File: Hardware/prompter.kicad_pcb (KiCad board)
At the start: 4 copper layers, 99.7 x 70.1 mm, 106 parts, among them J1 USB_B_Micro, J2 SWD, J3 L1, J4 L3, J5 PWR, J6 L2, J7 L4, J8 UART, J9 FootSW, Q1 AO3401A, Q2 IRLZ44N, Q3 IRLZ44N, Q4 IRLZ44N, Q5 IRLZ44N, SW1 PGM/RUN, SW2 SW_SPDT, SW3 SW_SPDT, SW4 SW_SPDT, SW5 SW_SPDT, U1 74HC14, U2 USBLC6-2P6, U3 STM32F405RGT6, U4 EL817, U5 EL817, U6 MP2359, Y1 16MHz

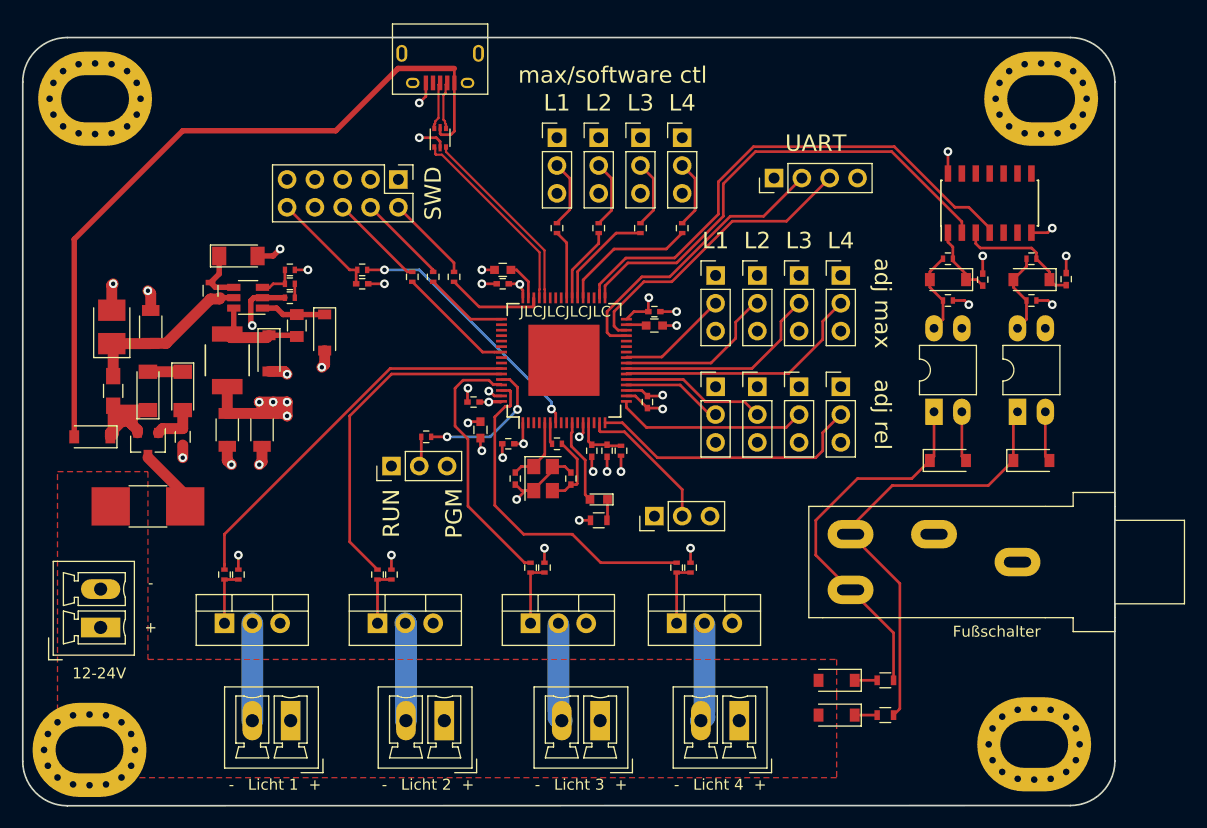
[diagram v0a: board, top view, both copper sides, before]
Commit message: for future extension, also added DMX hardware
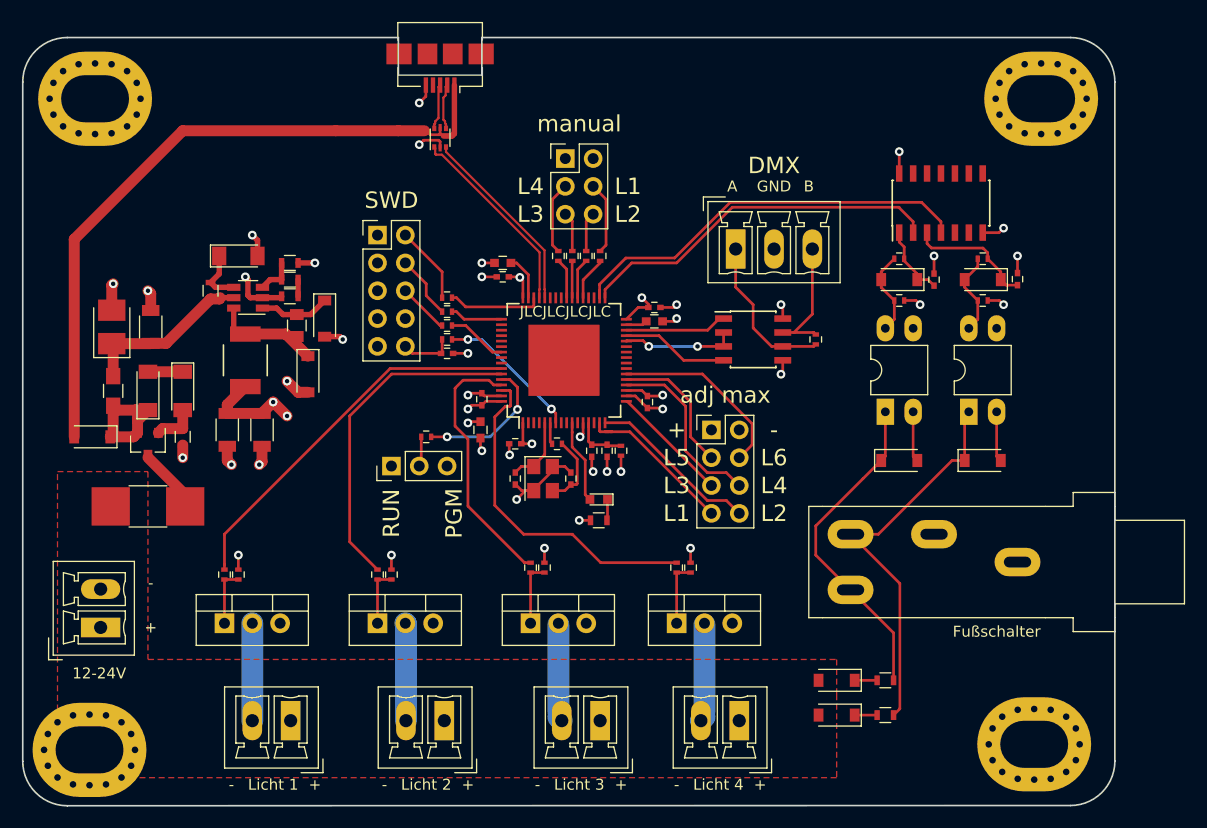
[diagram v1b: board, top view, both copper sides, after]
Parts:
- removed RV1, RV2, RV3, RV4, RV5, RV6, RV7, RV8, RV9: 10k, Pin_Headers:Pin_Header_Straight_1x03_Pitch2.54mm
- removed SW2, SW3, SW4, SW5: SW_SPDT, Pin_Headers:Pin_Header_Straight_1x03_Pitch2.54mm
- added J10: manual, Pin_Headers:Pin_Header_Straight_2x03_Pitch2.54mm, F.Cu at (74.4, 127.9)
- added J11: max, Pin_Headers:Pin_Header_Straight_2x04_Pitch2.54mm, F.Cu at (87.8, 152.7)
- added R31: 120, Resistors_SMD:R_0402, F.Cu at (97.3, 144.4)
- added U7: SP3485EN, Housings_SOIC:SOIC-8_3.9x4.9mm_Pitch1.27mm, F.Cu at (91.6, 144.4)
- J1: footprint Connectors:USB_Micro-B -> Connector_USB:USB_Micro-B_Amphenol_10104110_Horizontal
- J8: value UART -> DMX; footprint Pin_Headers:Pin_Header_Straight_1x04_Pitch2.54mm -> Connectors_Phoenix:PhoenixContact_MCV-G_03x3.50mm_Vertical
- R2, R4, R5: footprint Resistors_SMD:R_0402 -> Resistors_SMD:R_0603
- moved R13 11.6 mm to (73.8, 136.8)
- moved C6 10.0 mm to (63.6, 145.7)
- moved R9 10.0 mm to (63.6, 144.4)
- moved J8 7.36 mm to (90.0, 136.1), turned to 0 degrees
- moved R15 6.72 mm to (75.1, 136.8)
- moved R8 5.46 mm to (63.6, 143.1), turned to 180 degrees
- moved J2 5.43 mm to (57.3, 134.9), turned to 0 degrees
- moved C20 4.45 mm to (108.1, 138.9)
- moved U4 4.45 mm to (111.3, 151.0)
- moved C19 4.44 mm to (115.7, 138.9)
- moved D10 4.44 mm to (104.9, 138.9)
- moved D11 4.44 mm to (104.9, 155.4)
- moved D8 4.44 mm to (112.5, 155.4)
- moved D9 4.44 mm to (112.5, 138.9)
- moved R18 4.44 mm to (112.5, 140.8)
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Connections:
- J1 pad 4: Net-(J1-Pad4) -> (no net)
- J2 pad 7: Net-(J2-Pad7) -> (no net)
- J2 pad 8: Net-(J2-Pad8) -> (no net)
- J8 pad 1: +3V3 -> Net-(J8-Pad1)
- J8 pad 2: USART_TX -> GND
- J8 pad 3: USART_RX -> Net-(J8-Pad3)
- R13 pad 1: L1MAN -> L4MAN
- R14 pad 1: L3MAN -> L1MAN
- R15 pad 1: L2MAN -> L3MAN
- R16 pad 1: L4MAN -> L2MAN
- U3 pad 11: Net-(U3-Pad11) -> (no net)
- U3 pad 14: Net-(U3-Pad14) -> (no net)
- U3 pad 2: Net-(U3-Pad2) -> (no net)
- U3 pad 23: ADC7 -> (no net)
- U3 pad 24: ADC14 -> (no net)
- U3 pad 25: ADC15 -> (no net)
- U3 pad 26: Net-(U3-Pad26) -> (no net)
- U3 pad 27: Net-(U3-Pad27) -> (no net)
- U3 pad 28: Net-(U3-Pad28) -> DMX_RW
- U3 pad 3: Net-(U3-Pad3) -> (no net)
- U3 pad 35: Net-(U3-Pad35) -> (no net)
- U3 pad 36: Net-(U3-Pad36) -> (no net)
- U3 pad 4: Net-(U3-Pad4) -> (no net)
- U3 pad 41: Net-(U3-Pad41) -> (no net)
- U3 pad 42: Net-(U3-Pad42) -> (no net)
- U3 pad 43: Net-(U3-Pad43) -> (no net)
- U3 pad 50: Net-(U3-Pad50) -> (no net)
- U3 pad 51: Net-(U3-Pad51) -> (no net)
- U3 pad 52: Net-(U3-Pad52) -> (no net)
- U3 pad 53: Net-(U3-Pad53) -> (no net)
- U3 pad 54: Net-(U3-Pad54) -> (no net)
- U3 pad 56: Net-(U3-Pad56) -> (no net)
- U3 pad 57: Net-(U3-Pad57) -> (no net)
- U3 pad 8: Net-(U3-Pad8) -> (no net)
- U3 pad 9: Net-(U3-Pad9) -> (no net)
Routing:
- net ADC7: track 19.2 -> 0.00 mm
- net USART_RX: track 28.0 -> 9.31 mm
- net USART_TX: track 26.6 -> 9.80 mm
- net ADC14: track 15.1 -> 0.00 mm
- net Net-(J8-Pad1): track 0.00 -> 14.4 mm
- net Net-(J8-Pad3): track 0.00 -> 11.4 mm
- net NRST: track 23.9 -> 13.1 mm
- net FOOT_R_DB: track 44.1 -> 33.6 mm
- net DMX_RW: track 0.00 -> 10.4 mm, vias 0 -> 2
- net ADC15: track 10.2 -> 0.00 mm
- net FOOT_L_DB: track 47.9 -> 37.9 mm
- net ADC2: track 25.4 -> 15.7 mm
- net L1MAN: track 12.5 -> 4.02 mm
- net ADC4: track 9.26 -> 16.5 mm
- net ADC3: track 17.6 -> 10.9 mm
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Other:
- outline, holes or cut-outs redrawn
- board text added: "A"
- board text added: "B"
- board text added: "DMX"
- board text added: "GND"
- board text added: "L5"
- board text added: "L6"
- board text added: "manual"
- board text removed: "UART"
- board text removed: "adj rel"
- board text removed: "max/software ctl"

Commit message: Board updates:
Fixed footprints (SMD vs. THT, no hanging pads in the air)
Added mounting holes for production
Moved F.Fab text to readable locations
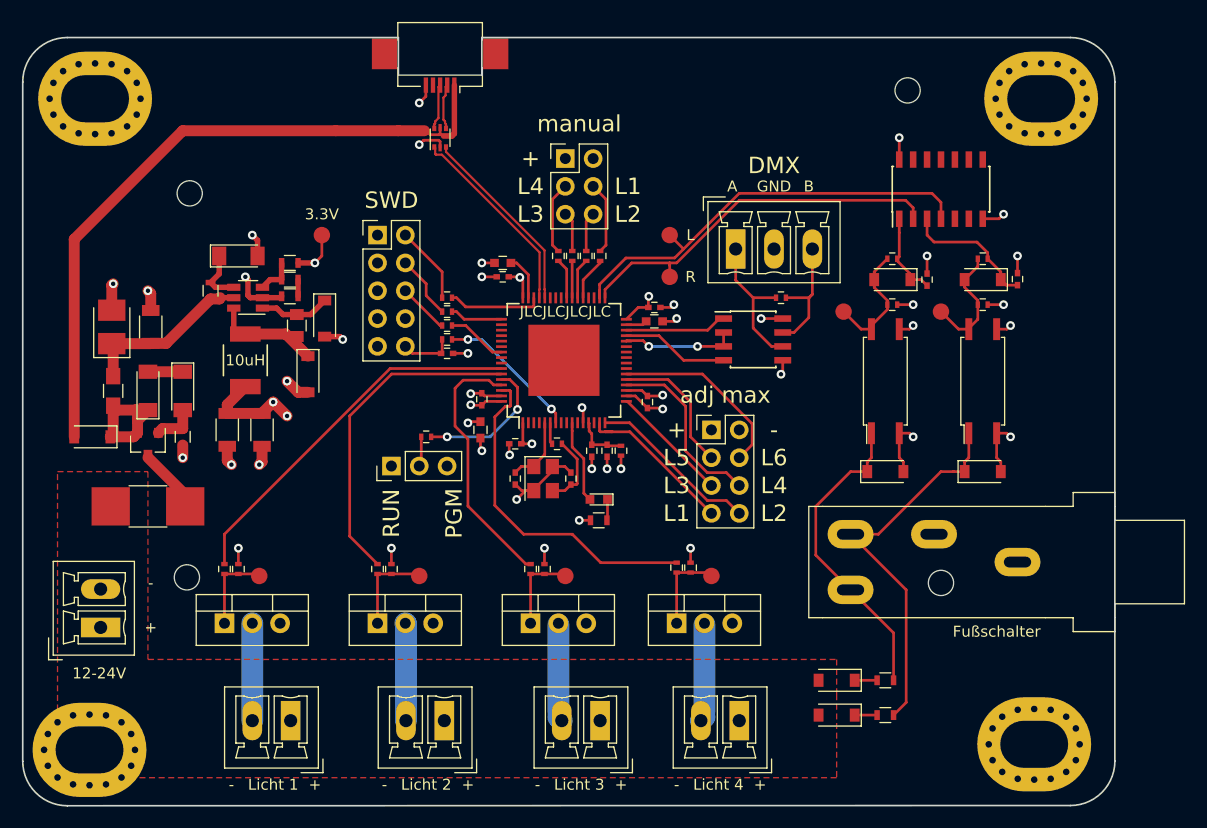
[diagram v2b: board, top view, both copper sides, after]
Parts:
- added  : 3.3V, Measurement_Points:Measurement_Point_Round-SMD-Pad_Small, F.Cu at (52.2, 134.9)
- added L: FootL, Measurement_Points:Measurement_Point_Round-SMD-Pad_Small, F.Cu at (83.9, 134.9)
- added R: FootR, Measurement_Points:Measurement_Point_Round-SMD-Pad_Small, F.Cu at (83.9, 138.7)
- added TP2: FootL, Measurement_Points:Measurement_Point_Round-SMD-Pad_Small, F.Cu at (108.7, 141.9)
- added TP3: FootR, Measurement_Points:Measurement_Point_Round-SMD-Pad_Small, F.Cu at (99.8, 141.9)
- added TP6: PWM, Measurement_Points:Measurement_Point_Round-SMD-Pad_Small, F.Cu at (46.5, 166.0)
- added TP7: PWM, Measurement_Points:Measurement_Point_Round-SMD-Pad_Small, F.Cu at (61.1, 166.0)
- added TP8: PWM, Measurement_Points:Measurement_Point_Round-SMD-Pad_Small, F.Cu at (74.4, 166.0)
- added TP9: PWM, Measurement_Points:Measurement_Point_Round-SMD-Pad_Small, F.Cu at (87.8, 166.0)
- J1: footprint Connector_USB:USB_Micro-B_Amphenol_10104110_Horizontal -> Hardware:USB_Micro-B
- U4, U5: footprint Housings_DIP:DIP-4_W7.62mm_LongPads -> Housings_SOIC:SO-4_7.6x3.6mm_Pitch2.54mm
- moved R31 4.96 mm to (94.1, 140.6), turned to 0 degrees
- moved U4 3.07 mm to (112.5, 148.2)
- moved U5 2.79 mm to (103.6, 148.2)
- moved D11 1.63 mm to (103.6, 156.5)
- moved U1 1.27 mm to (108.7, 130.7)
- moved D8 1.02 mm to (112.5, 156.5)
- moved R19 0.74 mm to (104.3, 141.2)
- moved C20 0.64 mm to (107.4, 138.9)
- moved D10 0.64 mm to (104.3, 138.9)
- moved R21 0.64 mm to (104.3, 137.0)
- moved R23 0.51 mm to (43.3, 165.4)
- moved R24 0.51 mm to (44.6, 165.4)
- moved R25 0.51 mm to (57.3, 165.4)
- moved R26 0.51 mm to (58.5, 165.4)
- moved R18 0.38 mm to (112.5, 141.2)
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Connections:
- J1 pad 4: (no net) -> Net-(J1-Pad4)
- J2 pad 7: (no net) -> Net-(J2-Pad7)
- J2 pad 8: (no net) -> Net-(J2-Pad8)
- U3 pad 11: (no net) -> Net-(U3-Pad11)
- U3 pad 14: (no net) -> Net-(U3-Pad14)
- U3 pad 2: (no net) -> Net-(U3-Pad2)
- U3 pad 23: (no net) -> Net-(U3-Pad23)
- U3 pad 24: (no net) -> Net-(U3-Pad24)
- U3 pad 25: (no net) -> Net-(U3-Pad25)
- U3 pad 26: (no net) -> Net-(U3-Pad26)
- U3 pad 27: (no net) -> Net-(U3-Pad27)
- U3 pad 3: (no net) -> Net-(U3-Pad3)
- U3 pad 35: (no net) -> Net-(U3-Pad35)
- U3 pad 36: (no net) -> Net-(U3-Pad36)
- U3 pad 4: (no net) -> Net-(U3-Pad4)
- U3 pad 41: (no net) -> Net-(U3-Pad41)
- U3 pad 42: (no net) -> Net-(U3-Pad42)
- U3 pad 43: (no net) -> Net-(U3-Pad43)
- U3 pad 50: (no net) -> Net-(U3-Pad50)
- U3 pad 51: (no net) -> Net-(U3-Pad51)
- U3 pad 52: (no net) -> Net-(U3-Pad52)
- U3 pad 53: (no net) -> Net-(U3-Pad53)
- U3 pad 54: (no net) -> Net-(U3-Pad54)
- U3 pad 56: (no net) -> Net-(U3-Pad56)
- U3 pad 57: (no net) -> Net-(U3-Pad57)
- U3 pad 8: (no net) -> Net-(U3-Pad8)
- U3 pad 9: (no net) -> Net-(U3-Pad9)
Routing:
- net FOOT_R: track 7.68 -> 11.2 mm
- net FOOT_L: track 7.68 -> 10.9 mm
- net Net-(Q3-Pad1): track 5.26 -> 8.26 mm
- net GND: track 103.3 -> 106.2 mm, vias 32 -> 36
- net Net-(Q2-Pad1): track 5.26 -> 7.75 mm
- net +3V3: track 38.5 -> 40.9 mm
- net FOOT_L_DB: track 37.9 -> 40.1 mm
- net Net-(Q4-Pad1): track 5.90 -> 7.75 mm
- net Net-(Q5-Pad1): track 5.90 -> 7.49 mm
- net FOOT_EXT_R: track 30.1 -> 28.5 mm
- net FOOT_R_DB: track 33.6 -> 34.8 mm
- net Net-(C20-Pad1): track 6.72 -> 7.88 mm
- net Net-(J8-Pad1): track 14.4 -> 13.4 mm
- net FOOT_EXT_L: track 36.6 -> 35.7 mm
- net Net-(C19-Pad1): track 11.6 -> 12.4 mm
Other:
- outline, holes or cut-outs redrawn
- board text added: "Prompter/Lichtsteuerung Christopher Creutzig, v0.1"

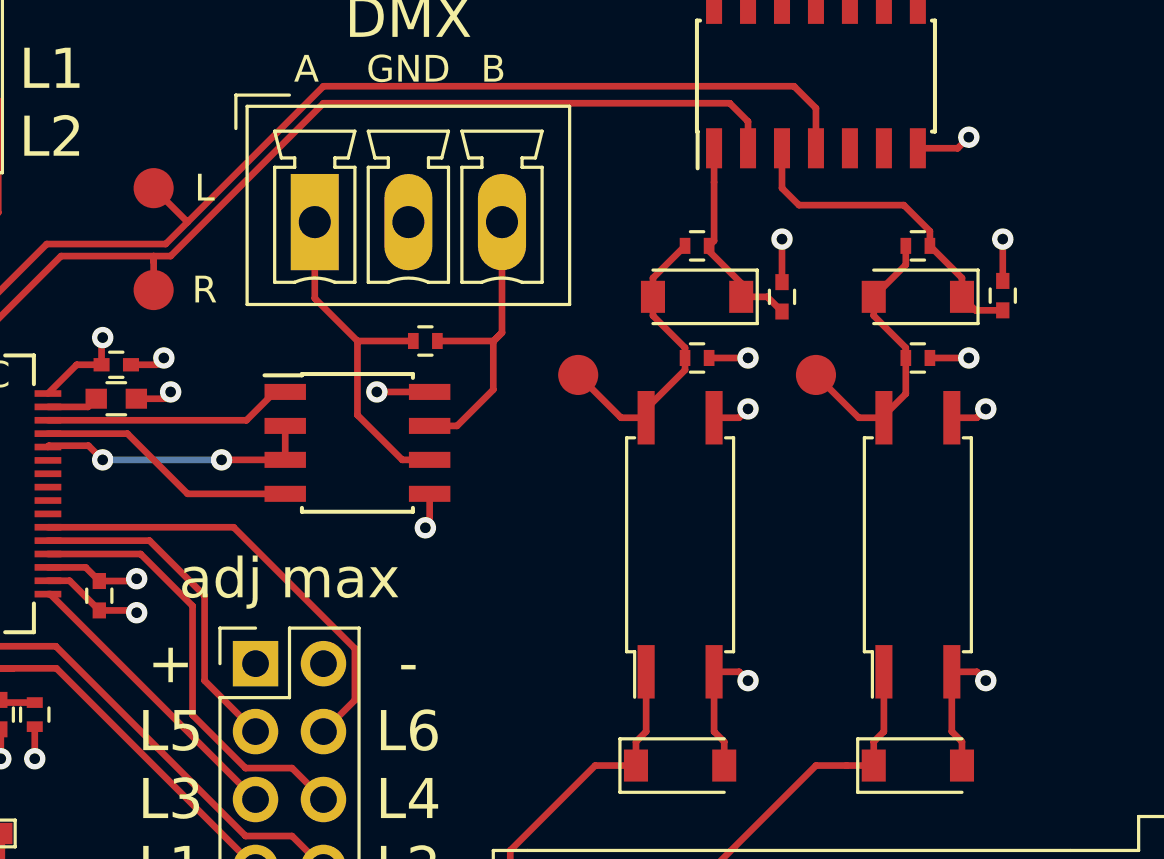
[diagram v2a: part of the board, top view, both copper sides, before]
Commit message: Hardware v0.1, Firmware runs ADC trigger by TIM3
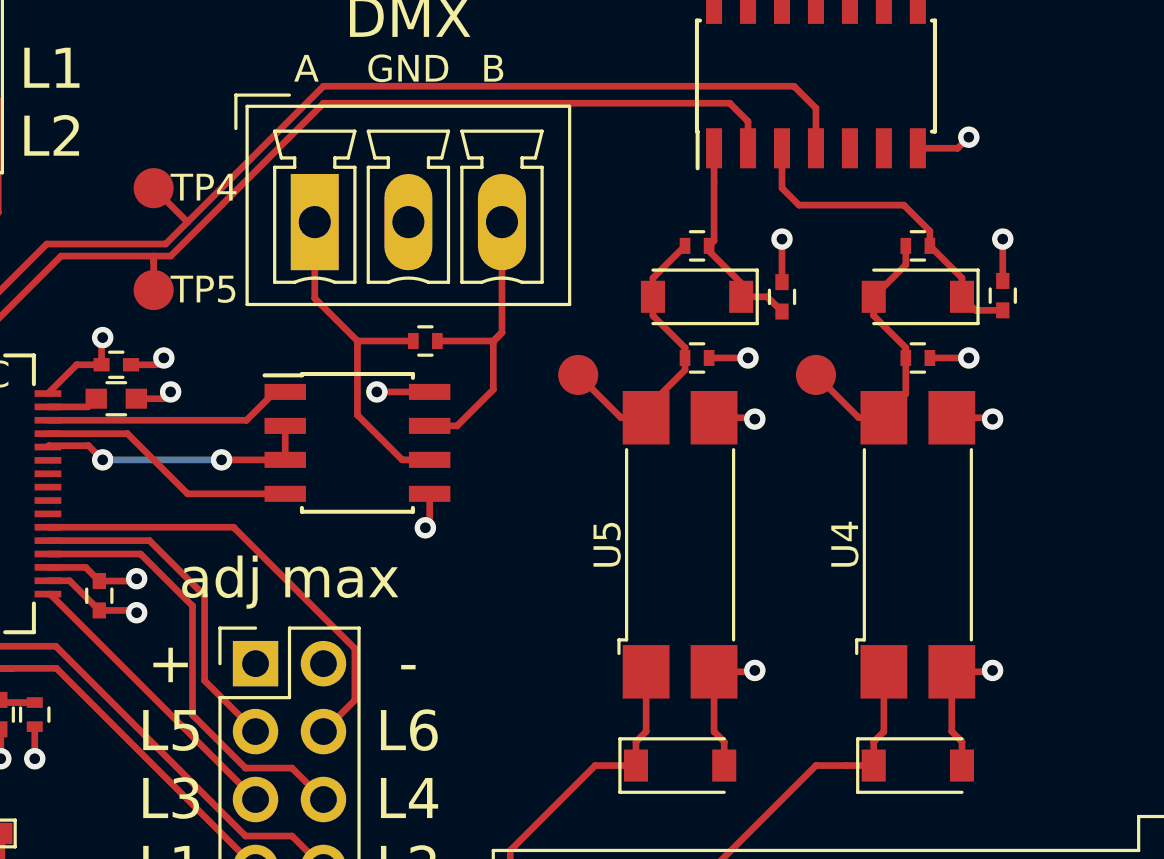
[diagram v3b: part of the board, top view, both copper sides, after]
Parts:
- TP1: renamed from  
- U4, U5: footprint Housings_SOIC:SO-4_7.6x3.6mm_Pitch2.54mm -> Hardware:SO-4_7.6x3.6mm_Pitch2.54mm
- renumbered L to TP4, R to TP5
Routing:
- net GND: track 106.2 -> 106.8 mm
